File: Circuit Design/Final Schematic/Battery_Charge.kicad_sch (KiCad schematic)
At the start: 10 parts

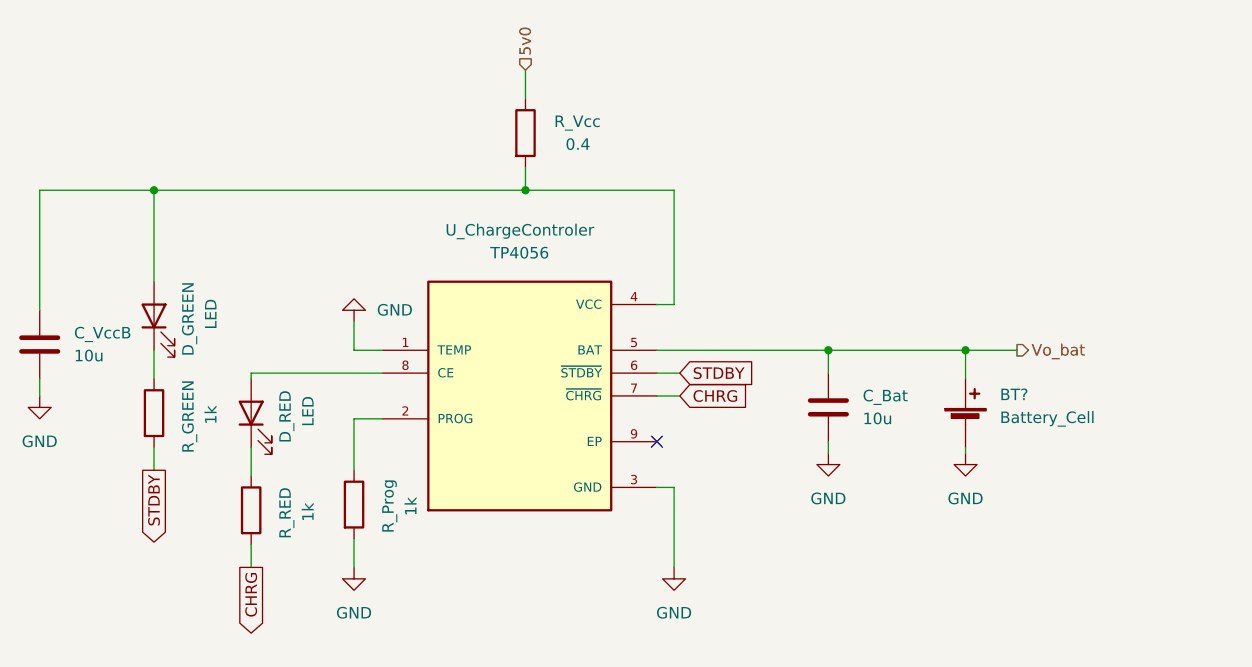
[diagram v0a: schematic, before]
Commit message: Power Module on schematic almost ready
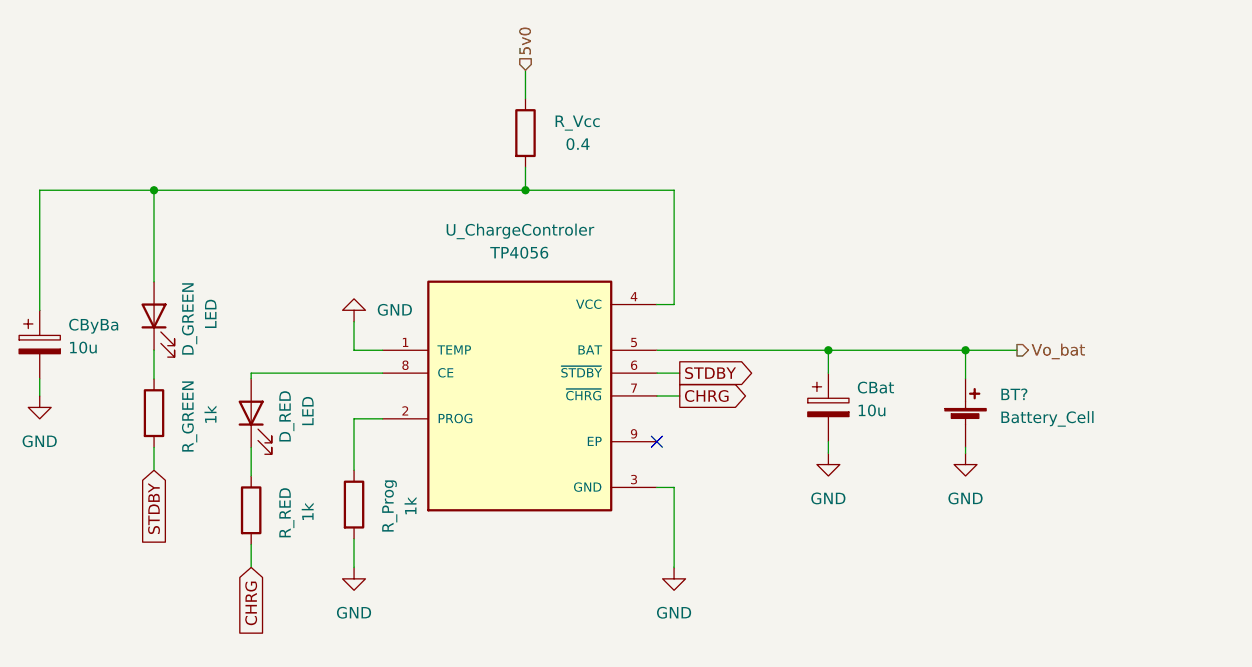
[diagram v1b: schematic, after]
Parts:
- removed C_Bat, C_VccB: 10u, symbol Device:C
- added CBat, CByBa: 10u, Capacitor_SMD:CP_Elec_6.3x5.8, symbol Device:C_Polarized
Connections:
- net GND: now also CBat.2, CByBa.2
- net Vo_bat: now also CBat.1
- net at D_GREEN.2 (A), R_Vcc.2, U_ChargeControler.4 (VCC): now also CByBa.1
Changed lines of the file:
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@@
     (stroke (width 0) (type default) (color 0 0 0 0))
   )
-  (global_label "CHRG" (shape output) (at 116.84 121.285 270) (fields_autoplaced)
+  (global_label "CHRG" (shape input) (at 116.84 121.285 270) (fields_autoplaced)
     (effects (font (size 1.27 1.27)) (justify right))
     (property "Intersheet References" "${INTERSHEET_REFS}" (id 0) (at 116.7606 128.8386 90)
@@
     )
   )
-  (global_label "CHRG" (shape input) (at 164.465 102.235 0) (fields_autoplaced)
+  (global_label "CHRG" (shape output) (at 164.465 102.235 0) (fields_autoplaced)
     (effects (font (size 1.27 1.27)) (justify left))
     (property "Intersheet References" "${INTERSHEET_REFS}" (id 0) (at 172.0186 102.1556 0)
@@
     )
   )
-  (global_label "STDBY" (shape output) (at 106.045 110.49 270) (fields_autoplaced)
+  (global_label "STDBY" (shape input) (at 106.045 110.49 270) (fields_autoplaced)
     (effects (font (size 1.27 1.27)) (justify right))
     (property "Intersheet References" "${INTERSHEET_REFS}" (id 0) (at 105.9656 118.7088 90)
@@
     )
   )
-  (global_label "STDBY" (shape input) (at 164.465 99.695 0) (fields_autoplaced)
+  (global_label "STDBY" (shape output) (at 164.465 99.695 0) (fields_autoplaced)
     (effects (font (size 1.27 1.27)) (justify left))
     (property "Intersheet References" "${INTERSHEET_REFS}" (id 0) (at 172.6838 99.6156 0)
@@
     (pin "9")
   )
+  (symbol (lib_id "Device:C_Polarized") (at 93.345 96.52 0) (unit 1)
+    (in_bom yes) (on_board yes) (fields_autoplaced)
+    (property "Reference" "CByBa" (id 0) (at 96.52 94.3609 0)
+      (effects (font (size 1.27 1.27)) (justify left))
+    )
+    (property "Value" "10u" (id 1) (at 96.52 96.9009 0)
+      (effects (font (size 1.27 1.27)) (justify left))
+    )
+    (property "Footprint" "Capacitor_SMD:CP_Elec_6.3x5.8" (id 2) (at 94.3102 100.33 0)
+      (effects (font (size 1.27 1.27)) hide)
+    )
+    (property "Datasheet" "~" (id 3) (at 93.345 96.52 0)
+      (effects (font (size 1.27 1.27)) hide)
+    )
+    (pin "1")
+    (pin "2")
+  )
+  (symbol (lib_id "Device:C_Polarized") (at 180.975 103.505 0) (unit 1)
+    (in_bom yes) (on_board yes) (fields_autoplaced)
+    (property "Reference" "CBat" (id 0) (at 184.15 101.3459 0)
+      (effects (font (size 1.27 1.27)) (justify left))
+    )
+    (property "Value" "10u" (id 1) (at 184.15 103.8859 0)
+      (effects (font (size 1.27 1.27)) (justify left))
+    )
+    (property "Footprint" "Capacitor_SMD:CP_Elec_6.3x5.8" (id 2) (at 181.9402 107.315 0)
+      (effects (font (size 1.27 1.27)) hide)
+    )
+    (property "Datasheet" "~" (id 3) (at 180.975 103.505 0)
+      (effects (font (size 1.27 1.27)) hide)
+    )
+    (pin "1")
+    (pin "2")
+  )
   (symbol (lib_id "Device:LED") (at 106.045 93.345 90) (unit 1)
     (in_bom yes) (on_board yes)
@@
       (effects (font (size 1.27 1.27)) hide)
     )
-    (pin "1")
-    (pin "2")
-  )
-  (symbol (lib_id "Device:C") (at 180.975 103.505 0) (unit 1)
-    (in_bom yes) (on_board yes) (fields_autoplaced)
-    (property "Reference" "C_Bat" (id 0) (at 184.785 102.2349 0)
-      (effects (font (size 1.27 1.27)) (justify left))
-    )
-    (property "Value" "10u" (id 1) (at 184.785 104.7749 0)
-      (effects (font (size 1.27 1.27)) (justify left))
-    )
-    (property "Footprint" "" (id 2) (at 181.9402 107.315 0)
-      (effects (font (size 1.27 1.27)) hide)
-    )
-    (property "Datasheet" "~" (id 3) (at 180.975 103.505 0)
-      (effects (font (size 1.27 1.27)) hide)
-    )
-    (pin "1")
-    (pin "2")
-  )
-  (symbol (lib_id "Device:C") (at 93.345 96.52 0) (unit 1)
-    (in_bom yes) (on_board yes) (fields_autoplaced)
-    (property "Reference" "C_VccB" (id 0) (at 97.155 95.2499 0)
-      (effects (font (size 1.27 1.27)) (justify left))
-    )
-    (property "Value" "10u" (id 1) (at 97.155 97.7899 0)
-      (effects (font (size 1.27 1.27)) (justify left))
-    )
-    (property "Footprint" "" (id 2) (at 94.3102 100.33 0)
-      (effects (font (size 1.27 1.27)) hide)
-    )
-    (property "Datasheet" "~" (id 3) (at 93.345 96.52 0)
-      (effects (font (size 1.27 1.27)) hide)
-    )

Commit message: Rprog changed
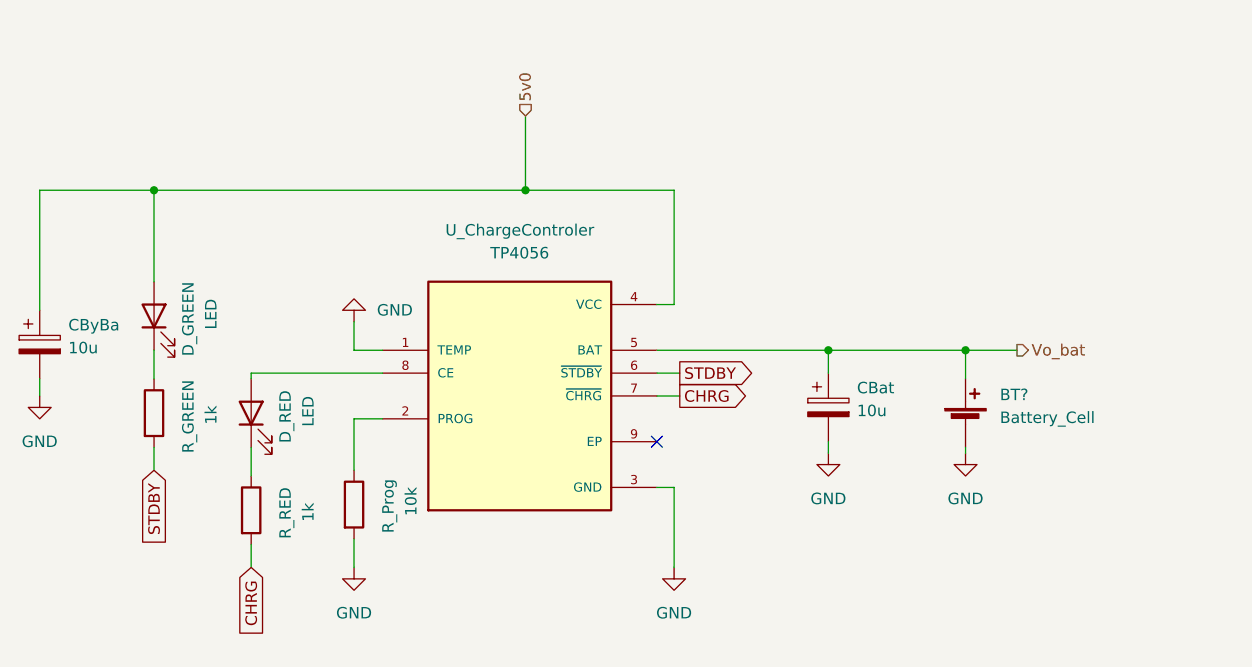
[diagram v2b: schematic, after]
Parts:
- removed R_Vcc: 0.4, symbol Device:R
- R_GREEN, R_RED: footprint (none) -> Resistor_SMD:R_0805_2012Metric_Pad1.20x1.40mm_HandSolder
- R_Prog: value 1k -> 10k; footprint (none) -> Resistor_SMD:R_0805_2012Metric_Pad1.20x1.40mm_HandSolder
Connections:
- net 5v0: now also CByBa.1, D_GREEN.2 (A), U_ChargeControler.4 (VCC)
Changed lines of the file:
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@@
-    (stroke (width 0) (type default) (color 0 0 0 0))
-  )
-  (wire (pts (xy 147.32 76.835) (xy 147.32 79.375))
     (stroke (width 0) (type default) (color 0 0 0 0))
   )
@@
     (stroke (width 0) (type default) (color 0 0 0 0))
   )
-  (wire (pts (xy 147.32 66.04) (xy 147.32 69.215))
+  (wire (pts (xy 147.32 71.12) (xy 147.32 79.375))
     (stroke (width 0) (type default) (color 0 0 0 0))
   )
@@
     (effects (font (size 1.27 1.27)) (justify left))
   )
-  (hierarchical_label "5v0" (shape input) (at 147.32 66.04 90)
+  (hierarchical_label "5v0" (shape input) (at 147.32 71.12 90)
     (effects (font (size 1.27 1.27)) (justify left))
   )
@@
       (effects (font (size 1.27 1.27)) (justify left))
     )
-    (property "Value" "1k" (id 1) (at 134.62 115.57 90)
-      (effects (font (size 1.27 1.27)) (justify left))
-    )
-    (property "Footprint" "" (id 2) (at 126.492 114.3 90)
+    (property "Value" "10k" (id 1) (at 134.62 115.57 90)
+      (effects (font (size 1.27 1.27)) (justify left))
+    )
+    (property "Footprint" "Resistor_SMD:R_0805_2012Metric_Pad1.20x1.40mm_HandSolder" (id 2) (at 126.492 114.3 90)
       (effects (font (size 1.27 1.27)) hide)
     )
@@
       (effects (font (size 1.27 1.27)) (justify left))
     )
-    (property "Footprint" "" (id 2) (at 115.062 114.935 90)
+    (property "Footprint" "Resistor_SMD:R_0805_2012Metric_Pad1.20x1.40mm_HandSolder" (id 2) (at 115.062 114.935 90)
       (effects (font (size 1.27 1.27)) hide)
     )
@@
     (pin "1")
   )
-  (symbol (lib_id "Device:R") (at 147.32 73.025 0) (unit 1)
-    (in_bom yes) (on_board yes)
-    (property "Reference" "R_Vcc" (id 0) (at 150.495 71.755 0)
-      (effects (font (size 1.27 1.27)) (justify left))
-    )
-    (property "Value" "0.4" (id 1) (at 151.765 74.295 0)
-      (effects (font (size 1.27 1.27)) (justify left))
-    )
-    (property "Footprint" "" (id 2) (at 145.542 73.025 90)
-      (effects (font (size 1.27 1.27)) hide)
-    )
-    (property "Datasheet" "~" (id 3) (at 147.32 73.025 0)
-      (effects (font (size 1.27 1.27)) hide)
-    )
-    (pin "1")
-    (pin "2")
-  )
   (symbol (lib_id "Device:LED") (at 116.84 104.14 90) (unit 1)
     (in_bom yes) (on_board yes)
@@
       (effects (font (size 1.27 1.27)) (justify left))
     )
-    (property "Footprint" "" (id 2) (at 104.267 104.14 90)
-      (effects (font (size 1.27 1.27)) hide)
-    )
+    (property "Footprint" "Resistor_SMD:R_0805_2012Metric_Pad1.20x1.40mm_HandSolder" (id 2) (at 104.267 104.14 90)
+      (effects (font (size 1.27 1.27)) hide)
+    )

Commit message: Boost
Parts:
- added BT2: Battery_Cell, Battery:BatteryHolder_MPD_BH-18650-PC2, symbol Device:Battery_Cell
- BT: renamed from BT?; footprint (none) -> Battery:BatteryHolder_MPD_BH-18650-PC2
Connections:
- net GND: now also BT2.2 (-)
- net Vo_bat: now also BT2.1 (+)
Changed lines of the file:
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@@
   (junction (at 147.32 79.375) (diameter 0) (color 0 0 0 0)
   )
+  (junction (at 207.645 97.155) (diameter 0) (color 0 0 0 0)
+  )
   (no_connect (at 161.925 107.315))
+  (wire (pts (xy 207.645 97.155) (xy 216.535 97.155))
+    (stroke (width 0) (type default) (color 0 0 0 0))
+  )
   (wire (pts (xy 180.975 97.155) (xy 180.975 99.695))
     (stroke (width 0) (type default) (color 0 0 0 0))
@@
     (stroke (width 0) (type default) (color 0 0 0 0))
   )
-  (wire (pts (xy 196.215 97.155) (xy 201.93 97.155))
+  (wire (pts (xy 196.215 97.155) (xy 207.645 97.155))
     (stroke (width 0) (type default) (color 0 0 0 0))
   )
@@
     (stroke (width 0) (type default) (color 0 0 0 0))
   )
+  (wire (pts (xy 207.645 107.95) (xy 207.645 108.585))
+    (stroke (width 0) (type default) (color 0 0 0 0))
+  )
   (wire (pts (xy 161.925 112.395) (xy 163.83 112.395))
     (stroke (width 0) (type default) (color 0 0 0 0))
@@
   )
   (wire (pts (xy 128.27 118.11) (xy 128.27 121.285))
+    (stroke (width 0) (type default) (color 0 0 0 0))
+  )
+  (wire (pts (xy 207.645 97.155) (xy 207.645 100.33))
     (stroke (width 0) (type default) (color 0 0 0 0))
   )
@@
     )
   )
-  (hierarchical_label "Vo_bat" (shape output) (at 201.93 97.155 0)
+  (hierarchical_label "Vo_bat" (shape output) (at 216.535 97.155 0)
     (effects (font (size 1.27 1.27)) (justify left))
   )
@@
     (pin "1")
   )
+  (symbol (lib_id "power:GND") (at 207.645 108.585 0) (unit 1)
+    (in_bom yes) (on_board yes) (fields_autoplaced)
+    (property "Reference" "#PWR?" (id 0) (at 207.645 114.935 0)
+      (effects (font (size 1.27 1.27)) hide)
+    )
+    (property "Value" "GND" (id 1) (at 207.645 113.665 0))
+    (property "Footprint" "" (id 2) (at 207.645 108.585 0)
+      (effects (font (size 1.27 1.27)) hide)
+    )
+    (property "Datasheet" "" (id 3) (at 207.645 108.585 0)
+      (effects (font (size 1.27 1.27)) hide)
+    )
+    (pin "1")
+  )
   (symbol (lib_id "power:GND") (at 93.345 102.235 0) (unit 1)
     (in_bom yes) (on_board yes) (fields_autoplaced)
@@
     )
     (pin "1")
+  )
+  (symbol (lib_id "Device:Battery_Cell") (at 207.645 105.41 0) (unit 1)
+    (in_bom yes) (on_board yes)
+    (property "Reference" "BT2" (id 0) (at 211.455 106.045 90)
+      (effects (font (size 1.27 1.27)) (justify left))
+    )
+    (property "Value" "Battery_Cell" (id 1) (at 213.995 109.22 90)
+      (effects (font (size 1.27 1.27)) (justify left))
+    )
+    (property "Footprint" "Battery:BatteryHolder_MPD_BH-18650-PC2" (id 2) (at 207.645 103.886 90)
+      (effects (font (size 1.27 1.27)) hide)
+    )
+    (property "Datasheet" "~" (id 3) (at 207.645 103.886 90)
+      (effects (font (size 1.27 1.27)) hide)
+    )
+    (pin "1")
+    (pin "2")
   )
   (symbol (lib_id "Device:LED") (at 116.84 104.14 90) (unit 1)
@@
   )
   (symbol (lib_id "Device:Battery_Cell") (at 196.215 105.41 0) (unit 1)
-    (in_bom yes) (on_board yes) (fields_autoplaced)
-    (property "Reference" "BT?" (id 0) (at 200.025 102.1079 0)
-      (effects (font (size 1.27 1.27)) (justify left))
-    )
-    (property "Value" "Battery_Cell" (id 1) (at 200.025 104.6479 0)
-      (effects (font (size 1.27 1.27)) (justify left))
-    )
-    (property "Footprint" "" (id 2) (at 196.215 103.886 90)
-      (effects (font (size 1.27 1.27)) hide)
-    )
+    (in_bom yes) (on_board yes)
+    (property "Reference" "BT" (id 0) (at 200.025 105.41 90)
+      (effects (font (size 1.27 1.27)) (justify left))
+    )
+    (property "Value" "Battery_Cell" (id 1) (at 201.93 109.855 90)
+      (effects (font (size 1.27 1.27)) (justify left))
+    )
+    (property "Footprint" "Battery:BatteryHolder_MPD_BH-18650-PC2" (id 2) (at 196.215 103.886 90)
+      (effects (font (size 1.27 1.27)) hide)
+    )

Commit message: Footprints
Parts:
- renumbered BT to BT1, CBat to CBat1, CByBa to CByBa1, D_GREEN to D_GREEN1, D_RED to D_RED1, R_GREEN to R_GREEN1, R_Prog to R_Prog1, R_RED to R_RED1, U_ChargeControler to U_ChargeControler1
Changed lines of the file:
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@@
   (symbol (lib_id "Device:R") (at 128.27 114.3 0) (unit 1)
     (in_bom yes) (on_board yes)
-    (property "Reference" "R_Prog" (id 0) (at 132.08 117.475 90)
+    (property "Reference" "R_Prog1" (id 0) (at 132.08 117.475 90)
       (effects (font (size 1.27 1.27)) (justify left))
     )
@@
   (symbol (lib_id "power:GND") (at 128.27 121.285 0) (unit 1)
     (in_bom yes) (on_board yes) (fields_autoplaced)
-    (property "Reference" "#PWR?" (id 0) (at 128.27 127.635 0)
+    (property "Reference" "#PWR0131" (id 0) (at 128.27 127.635 0)
       (effects (font (size 1.27 1.27)) hide)
     )
@@
   (symbol (lib_id "power:GND") (at 207.645 108.585 0) (unit 1)
     (in_bom yes) (on_board yes) (fields_autoplaced)
-    (property "Reference" "#PWR?" (id 0) (at 207.645 114.935 0)
+    (property "Reference" "#PWR0132" (id 0) (at 207.645 114.935 0)
       (effects (font (size 1.27 1.27)) hide)
     )
@@
   (symbol (lib_id "power:GND") (at 93.345 102.235 0) (unit 1)
     (in_bom yes) (on_board yes) (fields_autoplaced)
-    (property "Reference" "#PWR?" (id 0) (at 93.345 108.585 0)
+    (property "Reference" "#PWR0130" (id 0) (at 93.345 108.585 0)
       (effects (font (size 1.27 1.27)) hide)
     )
@@
   (symbol (lib_id "Device:R") (at 116.84 114.935 0) (unit 1)
     (in_bom yes) (on_board yes)
-    (property "Reference" "R_RED" (id 0) (at 120.65 118.11 90)
+    (property "Reference" "R_RED1" (id 0) (at 120.65 118.11 90)
       (effects (font (size 1.27 1.27)) (justify left))
     )
@@
   (symbol (lib_id "power:GND") (at 163.83 121.285 0) (unit 1)
     (in_bom yes) (on_board yes) (fields_autoplaced)
-    (property "Reference" "#PWR?" (id 0) (at 163.83 127.635 0)
+    (property "Reference" "#PWR0129" (id 0) (at 163.83 127.635 0)
       (effects (font (size 1.27 1.27)) hide)
     )
@@
   (symbol (lib_id "power:GND") (at 128.27 93.98 180) (unit 1)
     (in_bom yes) (on_board yes) (fields_autoplaced)
-    (property "Reference" "#PWR?" (id 0) (at 128.27 87.63 0)
+    (property "Reference" "#PWR0128" (id 0) (at 128.27 87.63 0)
       (effects (font (size 1.27 1.27)) hide)
     )
@@
   (symbol (lib_id "Device:LED") (at 116.84 104.14 90) (unit 1)
     (in_bom yes) (on_board yes)
-    (property "Reference" "D_RED" (id 0) (at 120.65 101.6 0)
+    (property "Reference" "D_RED1" (id 0) (at 120.65 101.6 0)
       (effects (font (size 1.27 1.27)) (justify right))
     )
@@
   (symbol (lib_id "Device:R") (at 106.045 104.14 0) (unit 1)
     (in_bom yes) (on_board yes)
-    (property "Reference" "R_GREEN" (id 0) (at 109.855 108.585 90)
+    (property "Reference" "R_GREEN1" (id 0) (at 109.855 108.585 90)
       (effects (font (size 1.27 1.27)) (justify left))
     )
@@
   (symbol (lib_id "power:GND") (at 180.975 108.585 0) (unit 1)
     (in_bom yes) (on_board yes) (fields_autoplaced)
-    (property "Reference" "#PWR?" (id 0) (at 180.975 114.935 0)
+    (property "Reference" "#PWR0134" (id 0) (at 180.975 114.935 0)
       (effects (font (size 1.27 1.27)) hide)
     )
@@
   (symbol (lib_id "TP4056:TP4056") (at 146.685 102.235 0) (unit 1)
     (in_bom yes) (on_board yes) (fields_autoplaced)
-    (property "Reference" "U_ChargeControler" (id 0) (at 146.685 83.82 0))
+    (property "Reference" "U_ChargeControler1" (id 0) (at 146.685 83.82 0))
     (property "Value" "TP4056" (id 1) (at 146.685 86.36 0))
     (property "Footprint" "TP4056_Bcharge:SOP127P600X175-9N" (id 2) (at 146.685 102.235 0)
@@
   (symbol (lib_id "Device:C_Polarized") (at 93.345 96.52 0) (unit 1)
     (in_bom yes) (on_board yes) (fields_autoplaced)
-    (property "Reference" "CByBa" (id 0) (at 96.52 94.3609 0)
+    (property "Reference" "CByBa1" (id 0) (at 96.52 94.3609 0)
       (effects (font (size 1.27 1.27)) (justify left))
     )
@@
   (symbol (lib_id "Device:C_Polarized") (at 180.975 103.505 0) (unit 1)
     (in_bom yes) (on_board yes) (fields_autoplaced)
-    (property "Reference" "CBat" (id 0) (at 184.15 101.3459 0)
+    (property "Reference" "CBat1" (id 0) (at 184.15 101.3459 0)
       (effects (font (size 1.27 1.27)) (justify left))
     )
@@
   (symbol (lib_id "Device:LED") (at 106.045 93.345 90) (unit 1)
     (in_bom yes) (on_board yes)
-    (property "Reference" "D_GREEN" (id 0) (at 109.855 89.535 0)
+    (property "Reference" "D_GREEN1" (id 0) (at 109.855 89.535 0)
       (effects (font (size 1.27 1.27)) (justify right))
     )
@@
   (symbol (lib_id "power:GND") (at 196.215 108.585 0) (unit 1)
     (in_bom yes) (on_board yes) (fields_autoplaced)
-    (property "Reference" "#PWR?" (id 0) (at 196.215 114.935 0)
+    (property "Reference" "#PWR0133" (id 0) (at 196.215 114.935 0)
       (effects (font (size 1.27 1.27)) hide)
     )
@@
   (symbol (lib_id "Device:Battery_Cell") (at 196.215 105.41 0) (unit 1)
     (in_bom yes) (on_board yes)
-    (property "Reference" "BT" (id 0) (at 200.025 105.41 90)
-      (effects (font (size 1.27 1.27)) (justify left))
-    )
+    (property "Reference" "BT1" (id 0) (at 200.025 105.41 90)
+      (effects (font (size 1.27 1.27)) (justify left))
+    )
